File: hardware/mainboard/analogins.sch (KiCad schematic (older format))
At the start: 24 parts, among them U13 MCP6004, U14 MCP6001-OT

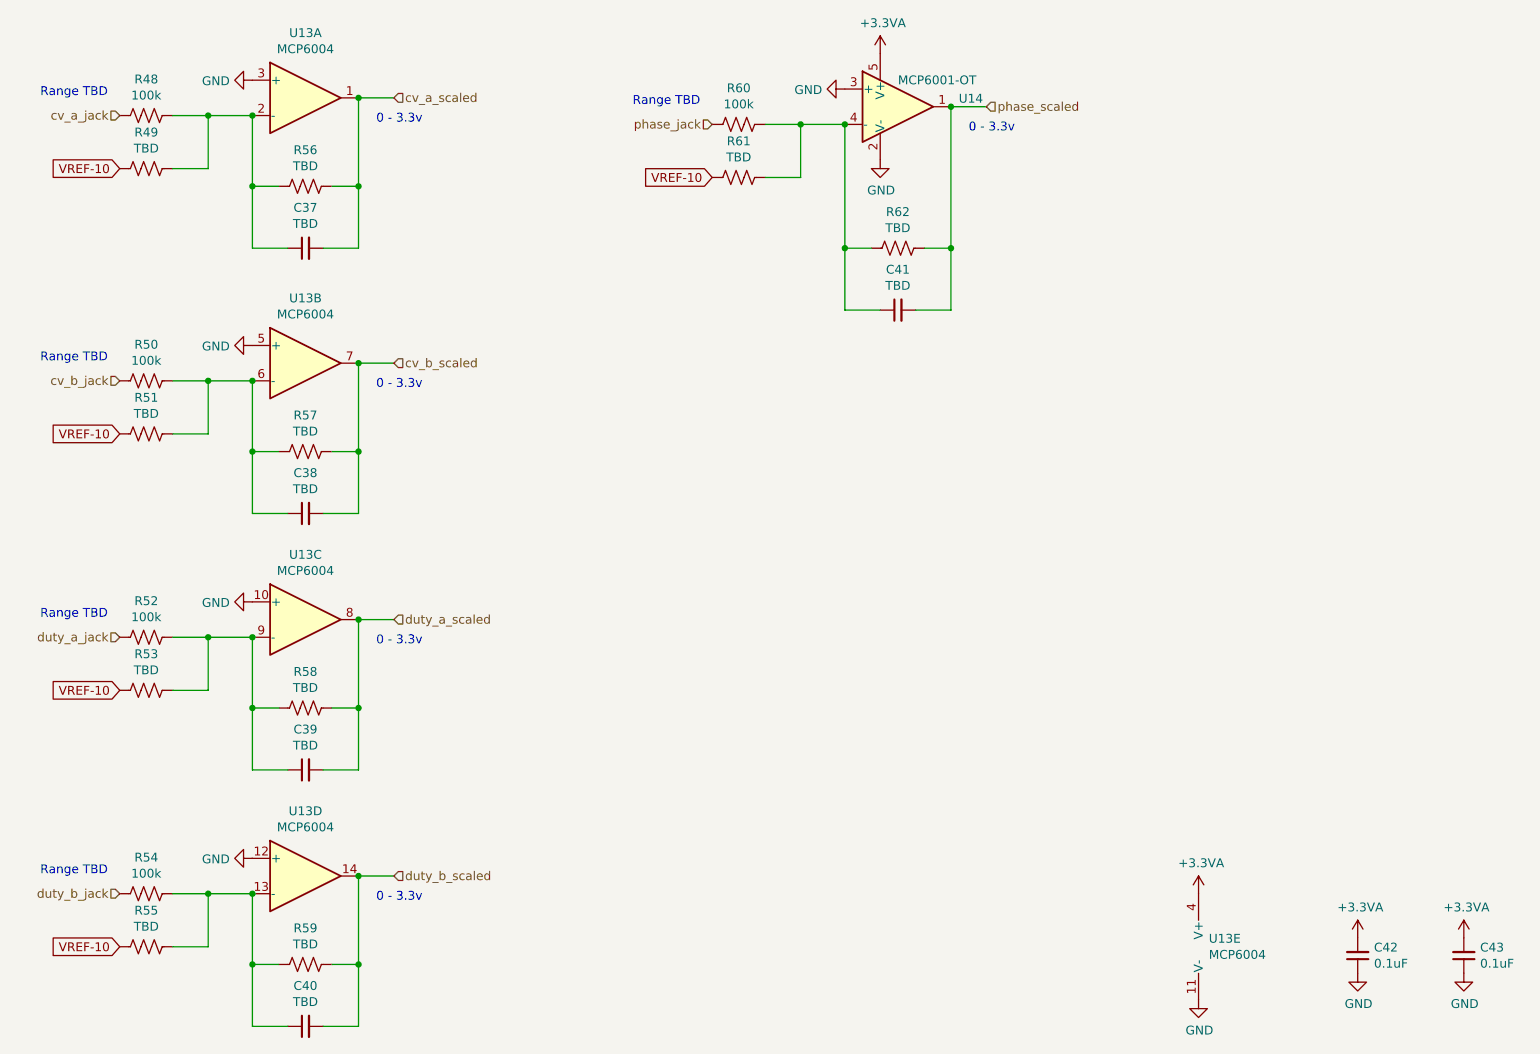
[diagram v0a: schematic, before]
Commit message: First pass layout & component selection for mainboard
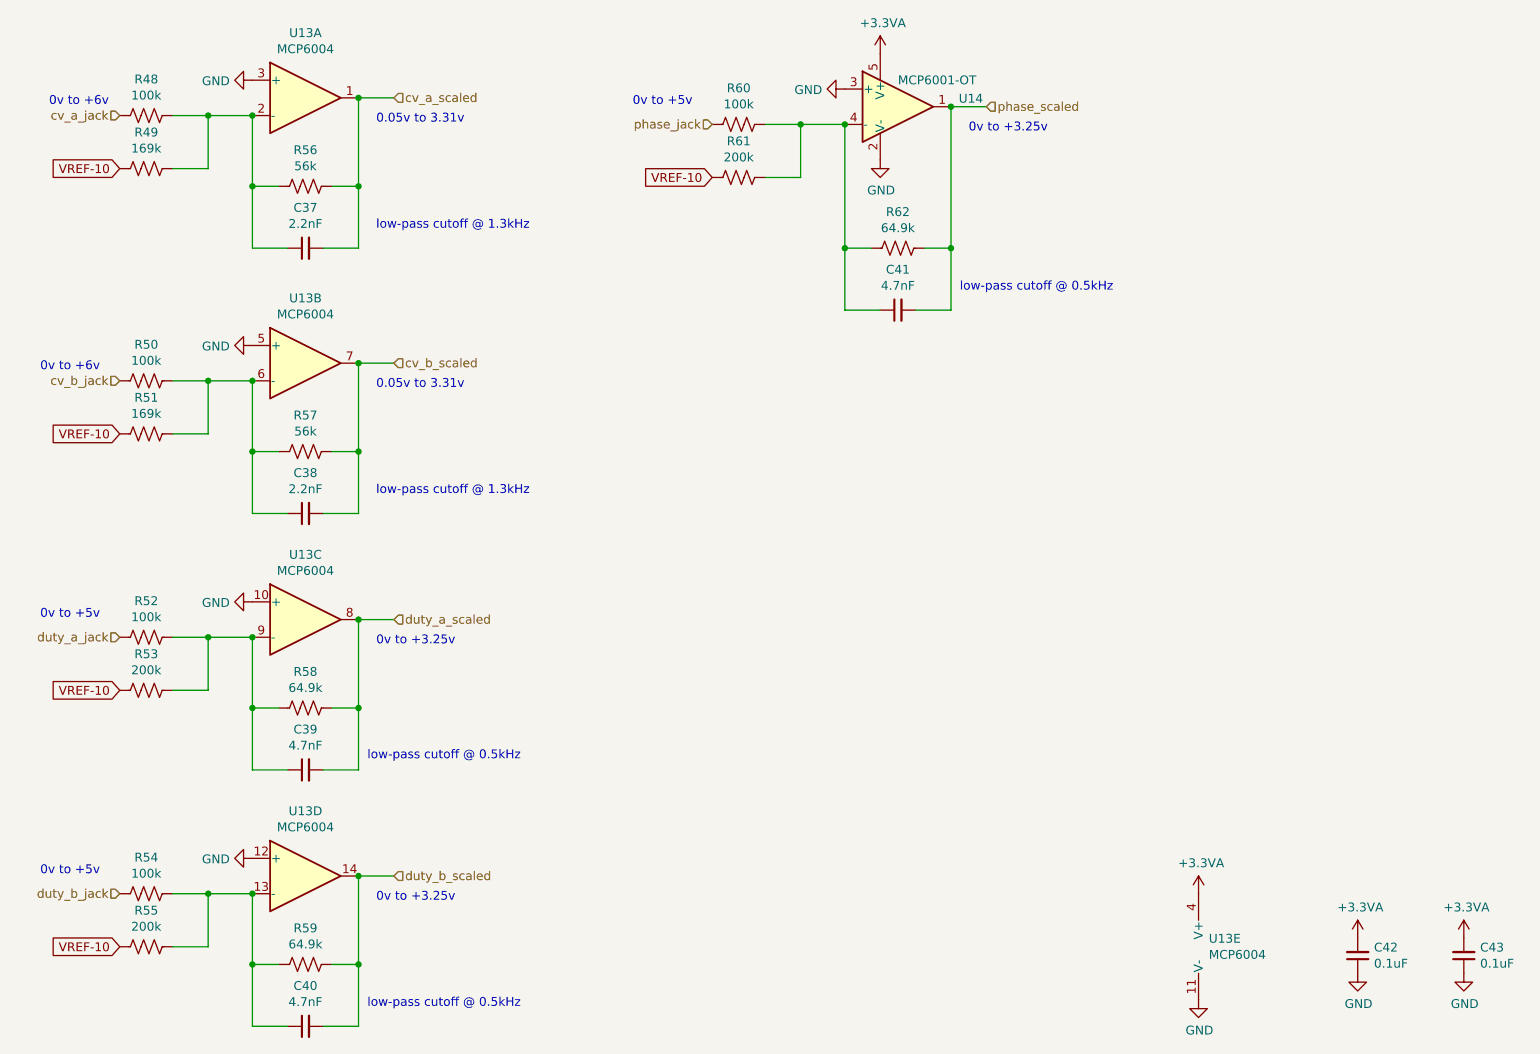
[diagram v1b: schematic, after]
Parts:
- C37, C38: value TBD -> 2.2nF; footprint Capacitor_SMD:C_0805_2012Metric_Pad1.15x1.40mm_HandSolder -> Capacitor_SMD:C_0603_1608Metric_Pad1.05x0.95mm_HandSolder; finalized no -> yes; mpn MF-CAP-0603-18pF -> GRM1885C1H222JA01D
- C39, C40, C41: value TBD -> 4.7nF; footprint Capacitor_SMD:C_0805_2012Metric_Pad1.15x1.40mm_HandSolder -> Capacitor_SMD:C_0603_1608Metric_Pad1.05x0.95mm_HandSolder; finalized no -> yes; mpn MF-CAP-0603-18pF -> MF-CAP-0603-4.7nF
- C42, C43: footprint Capacitor_SMD:C_0805_2012Metric_Pad1.15x1.40mm_HandSolder -> Capacitor_SMD:C_0603_1608Metric_Pad1.05x0.95mm_HandSolder; finalized no -> yes
- R48, R50, R52, R54, R60: footprint Resistor_SMD:R_1206_3216Metric_Pad1.42x1.75mm_HandSolder -> Resistor_SMD:R_0603_1608Metric_Pad1.05x0.95mm_HandSolder; Reqs (none) -> 0.5%; finalized no -> yes; mpn ERA8AEB222V -> ERA-3AED104V
- R49, R51: value TBD -> 169k; footprint Resistor_SMD:R_1206_3216Metric_Pad1.42x1.75mm_HandSolder -> Resistor_SMD:R_0603_1608Metric_Pad1.05x0.95mm_HandSolder; finalized no -> yes; mpn ERA8AEB222V -> ERA-3AEB1693V
- R53, R55, R61: value TBD -> 200k; footprint Resistor_SMD:R_1206_3216Metric_Pad1.42x1.75mm_HandSolder -> Resistor_SMD:R_0603_1608Metric_Pad1.05x0.95mm_HandSolder; finalized no -> yes; mpn ERA8AEB222V -> ERA-3AEB204V
- R56, R57: value TBD -> 56k; footprint Resistor_SMD:R_1206_3216Metric_Pad1.42x1.75mm_HandSolder -> Resistor_SMD:R_0603_1608Metric_Pad1.05x0.95mm_HandSolder; finalized no -> yes; mpn ERA8AEB222V -> ERA-3AEB563V
- R58, R59, R62: value TBD -> 64.9k; footprint Resistor_SMD:R_1206_3216Metric_Pad1.42x1.75mm_HandSolder -> Resistor_SMD:R_0603_1608Metric_Pad1.05x0.95mm_HandSolder; finalized no -> yes; mpn ERA8AEB222V -> ERA-3AEB6492V
- U13: finalized no -> yes; mpn MCP6004 -> MCP6004T-I/ST
- U14: finalized no -> yes
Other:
- note added: "0.05v to 3.31v"
- note added: "0v to +3.25v"
- note added: "0v to +5v"
- note added: "0v to +6v"
- note added: "low-pass cutoff @ 0.5kHz"
- note added: "low-pass cutoff @ 1.3kHz"
- note removed: "0 - 3.3v"
- note removed: "Range TBD"

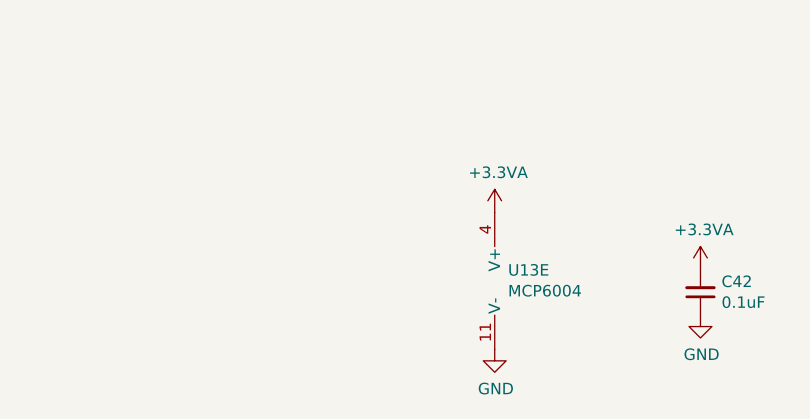
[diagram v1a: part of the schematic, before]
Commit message: Check passive ratings
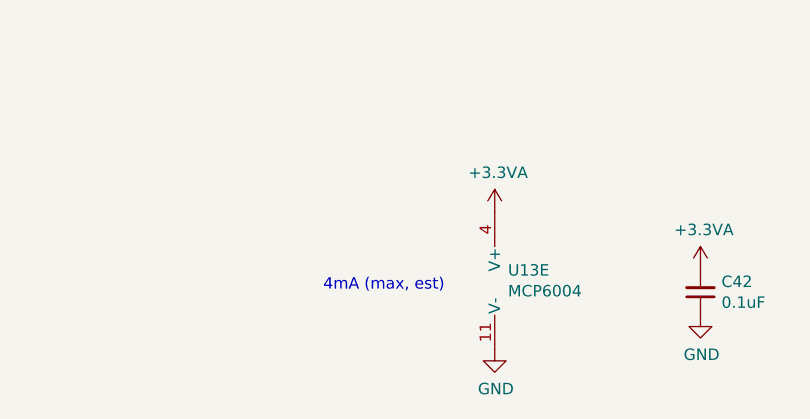
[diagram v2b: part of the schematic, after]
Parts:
- C37, C38: mpn specs (none) -> 5% 100v
- C39, C40, C41: mpn specs (none) -> 10% 50v
- C42, C43: mpn specs (none) -> 10%, 25v
- R48, R49, R50, R51, R52, R53, R54, R55, R56, R57, R58, R59, R60, R61, R62: mpn specs (none) -> 100mW
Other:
- note added: "4mA (max, est)"
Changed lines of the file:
@@
 F 1 "MCP6004" H 2400 1426 50  0000 C CNN
 F 2 "Package_SO:TSSOP-14_4.4x5mm_P0.65mm" H 2350 1250 50  0001 C CNN
-F 3 "http://ww1.microchip.com/downloads/en/DeviceDoc/21733j.pdf" H 2450 1350 50  0001 C CNN
+F 3 "http://ww1.microchip.com/downloads/en/DeviceDoc/MCP6001-1R-1U-2-4-1-MHz-Low-Power-Op-Amp-DS20001733L.pdf" H 2450 1350 50  0001 C CNN
 F 4 "yes" H 2400 1150 50  0001 C CNN "finalized"
 F 5 "MCP6004T-I/ST" H 2400 1150 50  0001 C CNN "mpn"
@@
 F 5 "ERA-3AED104V" H 1500 1250 50  0001 C CNN "mpn"
 F 6 "0.5%" H 1500 1250 50  0001 C CNN "Reqs"
+F 7 "100mW" H 1500 1250 50  0001 C CNN "mpn specs"
 	1    1500 1250
 	0    1    1    0
@@
 F 4 "yes" H 1500 1550 50  0001 C CNN "finalized"
 F 5 "ERA-3AEB1693V" H 1500 1550 50  0001 C CNN "mpn"
+F 6 "100mW" H 1500 1550 50  0001 C CNN "mpn specs"
 	1    1500 1550
 	0    1    1    0
@@
 F 4 "yes" H 2400 1650 50  0001 C CNN "finalized"
 F 5 "ERA-3AEB563V" H 2400 1650 50  0001 C CNN "mpn"
+F 6 "100mW" H 2400 1650 50  0001 C CNN "mpn specs"
 	1    2400 1650
 	0    1    1    0
@@
 F 4 "yes" H 2400 2000 50  0001 C CNN "finalized"
 F 5 "GRM1885C1H222JA01D" H 2400 2000 50  0001 C CNN "mpn"
+F 6 "5% 100v" H 2400 2000 50  0001 C CNN "mpn specs"
 	1    2400 2000
 	0    -1   -1   0
@@
 F 1 "MCP6004" H 2400 2926 50  0000 C CNN
 F 2 "Package_SO:TSSOP-14_4.4x5mm_P0.65mm" H 2350 2750 50  0001 C CNN
-F 3 "http://ww1.microchip.com/downloads/en/DeviceDoc/21733j.pdf" H 2450 2850 50  0001 C CNN
+F 3 "http://ww1.microchip.com/downloads/en/DeviceDoc/MCP6001-1R-1U-2-4-1-MHz-Low-Power-Op-Amp-DS20001733L.pdf" H 2450 2850 50  0001 C CNN
 F 4 "yes" H 2400 2650 50  0001 C CNN "finalized"
 F 5 "MCP6004T-I/ST" H 2400 2650 50  0001 C CNN "mpn"
@@
 F 5 "ERA-3AED104V" H 1500 2750 50  0001 C CNN "mpn"
 F 6 "0.5%" H 1500 2750 50  0001 C CNN "Reqs"
+F 7 "100mW" H 1500 2750 50  0001 C CNN "mpn specs"
 	1    1500 2750
 	0    1    1    0
@@
 F 4 "yes" H 1500 3050 50  0001 C CNN "finalized"
 F 5 "ERA-3AEB1693V" H 1500 3050 50  0001 C CNN "mpn"
+F 6 "100mW" H 1500 3050 50  0001 C CNN "mpn specs"
 	1    1500 3050
 	0    1    1    0
@@
 F 4 "yes" H 2400 3150 50  0001 C CNN "finalized"
 F 5 "ERA-3AEB563V" H 2400 3150 50  0001 C CNN "mpn"
+F 6 "100mW" H 2400 3150 50  0001 C CNN "mpn specs"
 	1    2400 3150
 	0    1    1    0
@@
 F 4 "yes" H 2400 3500 50  0001 C CNN "finalized"
 F 5 "GRM1885C1H222JA01D" H 2400 3500 50  0001 C CNN "mpn"
+F 6 "5% 100v" H 2400 3500 50  0001 C CNN "mpn specs"
 	1    2400 3500
 	0    -1   -1   0
@@
 F 1 "MCP6004" H 2400 4376 50  0000 C CNN
 F 2 "Package_SO:TSSOP-14_4.4x5mm_P0.65mm" H 2350 4200 50  0001 C CNN
-F 3 "http://ww1.microchip.com/downloads/en/DeviceDoc/21733j.pdf" H 2450 4300 50  0001 C CNN
+F 3 "http://ww1.microchip.com/downloads/en/DeviceDoc/MCP6001-1R-1U-2-4-1-MHz-Low-Power-Op-Amp-DS20001733L.pdf" H 2450 4300 50  0001 C CNN
 F 4 "yes" H 2400 4100 50  0001 C CNN "finalized"
 F 5 "MCP6004T-I/ST" H 2400 4100 50  0001 C CNN "mpn"
@@
 F 5 "ERA-3AED104V" H 1500 4200 50  0001 C CNN "mpn"
 F 6 "0.5%" H 1500 4200 50  0001 C CNN "Reqs"
+F 7 "100mW" H 1500 4200 50  0001 C CNN "mpn specs"
 	1    1500 4200
 	0    1    1    0
@@
 F 4 "yes" H 1500 4500 50  0001 C CNN "finalized"
 F 5 "ERA-3AEB204V" H 1500 4500 50  0001 C CNN "mpn"
+F 6 "100mW" H 1500 4500 50  0001 C CNN "mpn specs"
 	1    1500 4500
 	0    1    1    0
@@
 F 4 "yes" H 2400 4600 50  0001 C CNN "finalized"
 F 5 "ERA-3AEB6492V" H 2400 4600 50  0001 C CNN "mpn"
+F 6 "100mW" H 2400 4600 50  0001 C CNN "mpn specs"
 	1    2400 4600
 	0    1    1    0
@@
 F 4 "yes" H 2400 4950 50  0001 C CNN "finalized"
 F 5 "MF-CAP-0603-4.7nF" H 2400 4950 50  0001 C CNN "mpn"
+F 6 "10% 50v" H 2400 4950 50  0001 C CNN "mpn specs"
 	1    2400 4950
 	0    -1   -1   0
@@
 F 1 "MCP6004" H 2400 5826 50  0000 C CNN
 F 2 "Package_SO:TSSOP-14_4.4x5mm_P0.65mm" H 2350 5650 50  0001 C CNN
-F 3 "http://ww1.microchip.com/downloads/en/DeviceDoc/21733j.pdf" H 2450 5750 50  0001 C CNN
+F 3 "http://ww1.microchip.com/downloads/en/DeviceDoc/MCP6001-1R-1U-2-4-1-MHz-Low-Power-Op-Amp-DS20001733L.pdf" H 2450 5750 50  0001 C CNN
 F 4 "yes" H 2400 5550 50  0001 C CNN "finalized"
 F 5 "MCP6004T-I/ST" H 2400 5550 50  0001 C CNN "mpn"
@@
 F 5 "ERA-3AED104V" H 1500 5650 50  0001 C CNN "mpn"
 F 6 "0.5%" H 1500 5650 50  0001 C CNN "Reqs"
+F 7 "100mW" H 1500 5650 50  0001 C CNN "mpn specs"
 	1    1500 5650
 	0    1    1    0
@@
 F 4 "yes" H 1500 5950 50  0001 C CNN "finalized"
 F 5 "ERA-3AEB204V" H 1500 5950 50  0001 C CNN "mpn"
+F 6 "100mW" H 1500 5950 50  0001 C CNN "mpn specs"
 	1    1500 5950
 	0    1    1    0
@@
 F 4 "yes" H 2400 6050 50  0001 C CNN "finalized"
 F 5 "ERA-3AEB6492V" H 2400 6050 50  0001 C CNN "mpn"
+F 6 "100mW" H 2400 6050 50  0001 C CNN "mpn specs"
 	1    2400 6050
 	0    1    1    0
@@
 F 4 "yes" H 2400 6400 50  0001 C CNN "finalized"
 F 5 "MF-CAP-0603-4.7nF" H 2400 6400 50  0001 C CNN "mpn"
+F 6 "10% 50v" H 2400 6400 50  0001 C CNN "mpn specs"
 	1    2400 6400
 	0    -1   -1   0
@@
 F 5 "ERA-3AED104V" H 4850 1300 50  0001 C CNN "mpn"
 F 6 "0.5%" H 4850 1300 50  0001 C CNN "Reqs"
+F 7 "100mW" H 4850 1300 50  0001 C CNN "mpn specs"
 	1    4850 1300
 	0    1    1    0
@@
 F 4 "yes" H 4850 1600 50  0001 C CNN "finalized"
 F 5 "ERA-3AEB204V" H 4850 1600 50  0001 C CNN "mpn"
+F 6 "100mW" H 4850 1600 50  0001 C CNN "mpn specs"
 	1    4850 1600
 	0    1    1    0
@@
 F 4 "yes" H 5750 2000 50  0001 C CNN "finalized"
 F 5 "ERA-3AEB6492V" H 5750 2000 50  0001 C CNN "mpn"
+F 6 "100mW" H 5750 2000 50  0001 C CNN "mpn specs"
 	1    5750 2000
 	0    1    1    0
@@
 F 4 "yes" H 5750 2350 50  0001 C CNN "finalized"
 F 5 "MF-CAP-0603-4.7nF" H 5750 2350 50  0001 C CNN "mpn"
+F 6 "10% 50v" H 5750 2350 50  0001 C CNN "mpn specs"
 	1    5750 2350
 	0    -1   -1   0
@@
 F 1 "MCP6004" H 7508 5905 50  0000 L CNN
 F 2 "Package_SO:TSSOP-14_4.4x5mm_P0.65mm" H 7500 6050 50  0001 C CNN
-F 3 "http://ww1.microchip.com/downloads/en/DeviceDoc/21733j.pdf" H 7600 6150 50  0001 C CNN
+F 3 "http://ww1.microchip.com/downloads/en/DeviceDoc/MCP6001-1R-1U-2-4-1-MHz-Low-Power-Op-Amp-DS20001733L.pdf" H 7600 6150 50  0001 C CNN
 F 4 "yes" H 7550 5950 50  0001 C CNN "finalized"
 F 5 "MCP6004T-I/ST" H 7550 5950 50  0001 C CNN "mpn"
@@
 F 4 "yes" H 8350 6000 50  0001 C CNN "finalized"
 F 5 "MF-CAP-0603-0.1uF" H 8350 6000 50  0001 C CNN "mpn"
+F 6 "10%, 25v" H 8350 6000 50  0001 C CNN "mpn specs"
 	1    8350 6000
 	-1   0    0    1
@@
 F 4 "yes" H 8950 6000 50  0001 C CNN "finalized"
 F 5 "MF-CAP-0603-0.1uF" H 8950 6000 50  0001 C CNN "mpn"
+F 6 "10%, 25v" H 8950 6000 50  0001 C CNN "mpn specs"
 	1    8950 6000
 	-1   0    0    1
@@
 Text Notes 6100 2250 0    50   ~ 0
 low-pass cutoff @ 0.5kHz
+Text Notes 6700 6000 0    50   ~ 0
+4mA (max, est)
 $EndSCHEMATC

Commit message: Bumb schematics after generating gerbers and assigning alt mpns
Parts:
- C39, C40, C41: mpn alt (none) -> GRM1885C1H472JA01D
- C42, C43: mpn alt (none) -> GRM188R72A104KA35D
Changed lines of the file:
@@
 F 5 "MF-CAP-0603-4.7nF" H 2400 4950 50  0001 C CNN "mpn"
 F 6 "10% 50v" H 2400 4950 50  0001 C CNN "mpn specs"
+F 7 "GRM1885C1H472JA01D" H 2400 4950 50  0001 C CNN "mpn alt"
 	1    2400 4950
 	0    -1   -1   0
@@
 F 5 "MF-CAP-0603-4.7nF" H 2400 6400 50  0001 C CNN "mpn"
 F 6 "10% 50v" H 2400 6400 50  0001 C CNN "mpn specs"
+F 7 "GRM1885C1H472JA01D" H 2400 6400 50  0001 C CNN "mpn alt"
 	1    2400 6400
 	0    -1   -1   0
@@
 F 5 "MF-CAP-0603-4.7nF" H 5750 2350 50  0001 C CNN "mpn"
 F 6 "10% 50v" H 5750 2350 50  0001 C CNN "mpn specs"
+F 7 "GRM1885C1H472JA01D" H 5750 2350 50  0001 C CNN "mpn alt"
 	1    5750 2350
 	0    -1   -1   0
@@
 F 5 "MF-CAP-0603-0.1uF" H 8350 6000 50  0001 C CNN "mpn"
 F 6 "10%, 25v" H 8350 6000 50  0001 C CNN "mpn specs"
+F 7 "GRM188R72A104KA35D" H 8350 6000 50  0001 C CNN "mpn alt"
 	1    8350 6000
 	-1   0    0    1
@@
 F 5 "MF-CAP-0603-0.1uF" H 8950 6000 50  0001 C CNN "mpn"
 F 6 "10%, 25v" H 8950 6000 50  0001 C CNN "mpn specs"
+F 7 "GRM188R72A104KA35D" H 8950 6000 50  0001 C CNN "mpn alt"
 	1    8950 6000
 	-1   0    0    1

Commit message: Fix incorrect MPN for 10uF cap
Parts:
- C39, C40, C41: mpn alt GRM1885C1H472JA01D -> GRM21BR61E106KA73K
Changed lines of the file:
@@
 F 5 "MF-CAP-0603-4.7nF" H 2400 4950 50  0001 C CNN "mpn"
 F 6 "10% 50v" H 2400 4950 50  0001 C CNN "mpn specs"
-F 7 "GRM1885C1H472JA01D" H 2400 4950 50  0001 C CNN "mpn alt"
+F 7 "GRM21BR61E106KA73K" H 2400 4950 50  0001 C CNN "mpn alt"
 	1    2400 4950
 	0    -1   -1   0
@@
 F 5 "MF-CAP-0603-4.7nF" H 2400 6400 50  0001 C CNN "mpn"
 F 6 "10% 50v" H 2400 6400 50  0001 C CNN "mpn specs"
-F 7 "GRM1885C1H472JA01D" H 2400 6400 50  0001 C CNN "mpn alt"
+F 7 "GRM21BR61E106KA73K" H 2400 6400 50  0001 C CNN "mpn alt"
 	1    2400 6400
 	0    -1   -1   0
@@
 F 5 "MF-CAP-0603-4.7nF" H 5750 2350 50  0001 C CNN "mpn"
 F 6 "10% 50v" H 5750 2350 50  0001 C CNN "mpn specs"
-F 7 "GRM1885C1H472JA01D" H 5750 2350 50  0001 C CNN "mpn alt"
+F 7 "GRM21BR61E106KA73K" H 5750 2350 50  0001 C CNN "mpn alt"
 	1    5750 2350
 	0    -1   -1   0

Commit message: Fix a few more mpns
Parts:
- C37, C38: mpn GRM1885C1H222JA01D -> GRM1885C1H222JA01J
- C39, C40, C41: mpn alt GRM21BR61E106KA73K -> GCD188R71H472MA01D
- C42, C43: mpn alt GRM188R72A104KA35D -> GCM188R91E104KA37D
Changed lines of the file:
@@
 F 3 "~" H 2400 2000 50  0001 C CNN
 F 4 "yes" H 2400 2000 50  0001 C CNN "finalized"
-F 5 "GRM1885C1H222JA01D" H 2400 2000 50  0001 C CNN "mpn"
+F 5 "GRM1885C1H222JA01J" H 2400 2000 50  0001 C CNN "mpn"
 F 6 "5% 100v" H 2400 2000 50  0001 C CNN "mpn specs"
 	1    2400 2000
@@
 F 3 "~" H 2400 3500 50  0001 C CNN
 F 4 "yes" H 2400 3500 50  0001 C CNN "finalized"
-F 5 "GRM1885C1H222JA01D" H 2400 3500 50  0001 C CNN "mpn"
+F 5 "GRM1885C1H222JA01J" H 2400 3500 50  0001 C CNN "mpn"
 F 6 "5% 100v" H 2400 3500 50  0001 C CNN "mpn specs"
 	1    2400 3500
@@
 F 5 "MF-CAP-0603-4.7nF" H 2400 4950 50  0001 C CNN "mpn"
 F 6 "10% 50v" H 2400 4950 50  0001 C CNN "mpn specs"
-F 7 "GRM21BR61E106KA73K" H 2400 4950 50  0001 C CNN "mpn alt"
+F 7 "GCD188R71H472MA01D" H 2400 4950 50  0001 C CNN "mpn alt"
 	1    2400 4950
 	0    -1   -1   0
@@
 F 5 "MF-CAP-0603-4.7nF" H 2400 6400 50  0001 C CNN "mpn"
 F 6 "10% 50v" H 2400 6400 50  0001 C CNN "mpn specs"
-F 7 "GRM21BR61E106KA73K" H 2400 6400 50  0001 C CNN "mpn alt"
+F 7 "GCD188R71H472MA01D" H 2400 6400 50  0001 C CNN "mpn alt"
 	1    2400 6400
 	0    -1   -1   0
@@
 F 5 "MF-CAP-0603-4.7nF" H 5750 2350 50  0001 C CNN "mpn"
 F 6 "10% 50v" H 5750 2350 50  0001 C CNN "mpn specs"
-F 7 "GRM21BR61E106KA73K" H 5750 2350 50  0001 C CNN "mpn alt"
+F 7 "GCD188R71H472MA01D" H 5750 2350 50  0001 C CNN "mpn alt"
 	1    5750 2350
 	0    -1   -1   0
@@
 F 5 "MF-CAP-0603-0.1uF" H 8350 6000 50  0001 C CNN "mpn"
 F 6 "10%, 25v" H 8350 6000 50  0001 C CNN "mpn specs"
-F 7 "GRM188R72A104KA35D" H 8350 6000 50  0001 C CNN "mpn alt"
+F 7 "GCM188R91E104KA37D" H 8350 6000 50  0001 C CNN "mpn alt"
 	1    8350 6000
 	-1   0    0    1
@@
 F 5 "MF-CAP-0603-0.1uF" H 8950 6000 50  0001 C CNN "mpn"
 F 6 "10%, 25v" H 8950 6000 50  0001 C CNN "mpn specs"
-F 7 "GRM188R72A104KA35D" H 8950 6000 50  0001 C CNN "mpn alt"
+F 7 "GCM188R91E104KA37D" H 8950 6000 50  0001 C CNN "mpn alt"
 	1    8950 6000
 	-1   0    0    1
